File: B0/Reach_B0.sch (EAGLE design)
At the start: 149 parts, among them IC1 TMC2100-LA, IC18 74AHC1G126DCK, IC2 TMC2100-LA, IC3 74AHC1G126DCK, IC4 74AHC1G126DCK, IC5 74AHC1G126DCK, IC6 74AHC1G126DCK, IC7 74AHC1G126DCK, P8 F-2X23-, P9 F-2X23-, Q2 AON6758, Q3 AON6758, U1 SN74AHC595PW, U10 RT8268, U11 PCA9685PW, U18 CAT24C256, U2 SN74AHC595PW, U3 MCP9600, U4 MCP9600, U5 MCP9600, U6 MCP9600, X1 22-05-7028-02, X11 22-05-7028-02, X14 22-05-7048-04, X2 MSTBA4, X21 MSTBA2, X3 MSTBA2, X4 22-05-7028-02, X5 22-05-7028-02, X6 22-05-7048-04, X7 22-05-7028-02, X9 22-05-7028-02

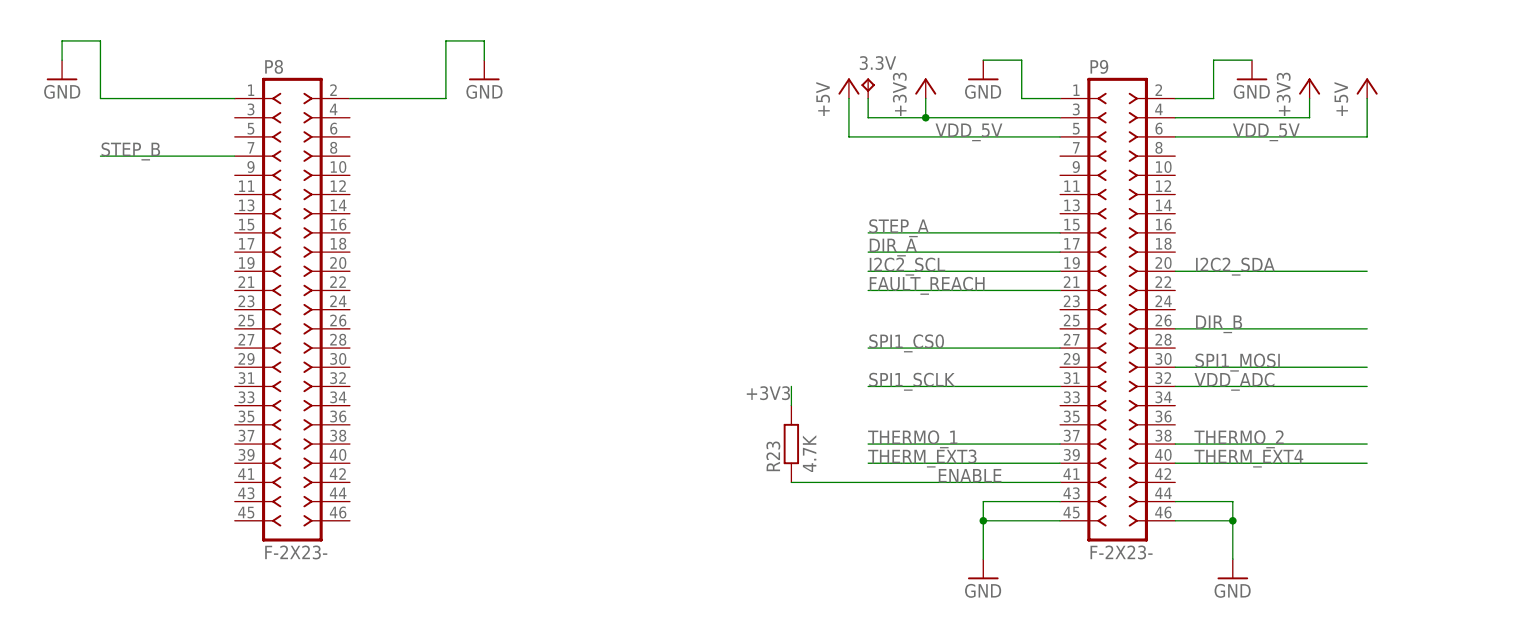
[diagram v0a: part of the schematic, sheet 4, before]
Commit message: multisheet schematic changes
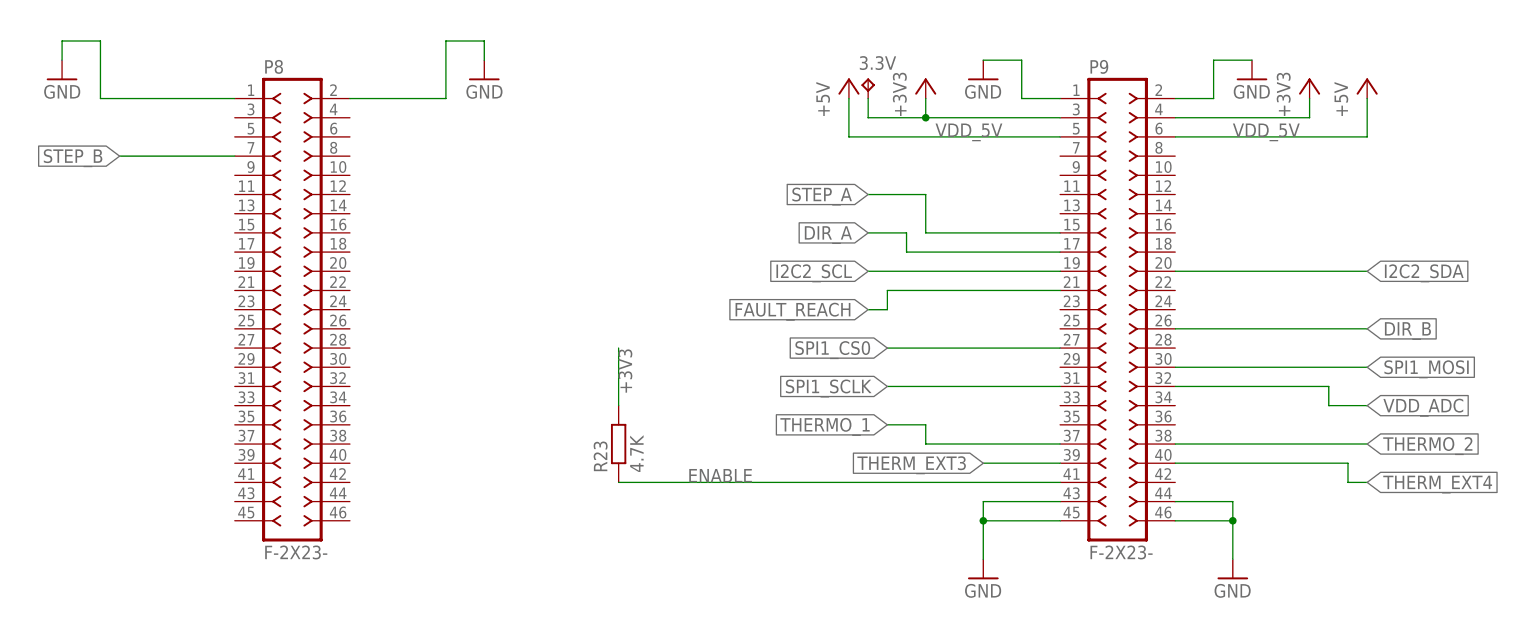
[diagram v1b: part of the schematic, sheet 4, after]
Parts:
- R13, R22, R26: value (none) -> 10k
- R16: value (none) -> 2.2k
- R24: value (none) -> 4.3k
- R27: value (none) -> 7.5k
- R7: value (none) -> DNP
- R8: value (none) -> 0
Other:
- moved on the sheet: R23
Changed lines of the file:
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@@
 <part name="GND12" library="supply1" deviceset="GND" device=""/>
 <part name="+3V8" library="supply1" deviceset="+3V3" device=""/>
-<part name="R7" library="SparkFun-Resistors" deviceset="RESISTOR" device="0402-RES"/>
-<part name="R8" library="SparkFun-Resistors" deviceset="RESISTOR" device="0402-RES"/>
+<part name="R7" library="SparkFun-Resistors" deviceset="RESISTOR" device="0402-RES" value="DNP"/>
+<part name="R8" library="SparkFun-Resistors" deviceset="RESISTOR" device="0402-RES" value="0"/>
 <part name="+3V10" library="supply1" deviceset="+3V3" device=""/>
 <part name="XTC2" library="reach_custom" deviceset="NEWPORT_THERMOCOUPLE_CONNECTOR" device="PCC-SMP-V"/>
@@
 <part name="GND13" library="supply1" deviceset="GND" device=""/>
 <part name="+3V11" library="supply1" deviceset="+3V3" device=""/>
-<part name="R13" library="SparkFun-Resistors" deviceset="RESISTOR" device="0402-RES"/>
-<part name="R16" library="SparkFun-Resistors" deviceset="RESISTOR" device="0402-RES"/>
+<part name="R13" library="SparkFun-Resistors" deviceset="RESISTOR" device="0402-RES" value="10k"/>
+<part name="R16" library="SparkFun-Resistors" deviceset="RESISTOR" device="0402-RES" value="2.2k"/>
 <part name="+3V13" library="supply1" deviceset="+3V3" device=""/>
 <part name="XTC3" library="reach_custom" deviceset="NEWPORT_THERMOCOUPLE_CONNECTOR" device="PCC-SMP-V"/>
@@
 <part name="GND30" library="supply1" deviceset="GND" device=""/>
 <part name="+3V14" library="supply1" deviceset="+3V3" device=""/>
-<part name="R22" library="SparkFun-Resistors" deviceset="RESISTOR" device="0402-RES"/>
-<part name="R24" library="SparkFun-Resistors" deviceset="RESISTOR" device="0402-RES"/>
+<part name="R22" library="SparkFun-Resistors" deviceset="RESISTOR" device="0402-RES" value="10k"/>
+<part name="R24" library="SparkFun-Resistors" deviceset="RESISTOR" device="0402-RES" value="4.3k"/>
 <part name="+3V15" library="supply1" deviceset="+3V3" device=""/>
 <part name="XTC4" library="reach_custom" deviceset="NEWPORT_THERMOCOUPLE_CONNECTOR" device="PCC-SMP-V"/>
@@
 <part name="GND33" library="supply1" deviceset="GND" device=""/>
 <part name="+3V16" library="supply1" deviceset="+3V3" device=""/>
-<part name="R26" library="SparkFun-Resistors" deviceset="RESISTOR" device="0402-RES"/>
-<part name="R27" library="SparkFun-Resistors" deviceset="RESISTOR" device="0402-RES"/>
+<part name="R26" library="SparkFun-Resistors" deviceset="RESISTOR" device="0402-RES" value="10k"/>
+<part name="R27" library="SparkFun-Resistors" deviceset="RESISTOR" device="0402-RES" value="7.5k"/>
 <part name="+3V17" library="supply1" deviceset="+3V3" device=""/>
 <part name="C9" library="rcl" deviceset="C-EU" device="C0402" value="0.1uF"/>
@@
 <instance part="P8" gate="G$1" x="63.5" y="58.42"/>
 <instance part="P9" gate="G$1" x="172.72" y="58.42"/>
-<instance part="R23" gate="G$1" x="129.54" y="40.64" rot="R90"/>
+<instance part="R23" gate="G$1" x="106.68" y="40.64" rot="R90"/>
 </instances>
 <busses>
@@
 <segment>
 <wire x1="165.1" y1="63.5" x2="139.7" y2="63.5" width="0.1524" layer="91"/>
-<label x="139.7" y="63.5" size="1.778" layer="95"/>
+<label x="139.7" y="63.5" size="1.778" layer="95" rot="R180" xref="yes"/>
 <pinref part="P9" gate="G$1" pin="19"/>
 </segment>
@@
 <segment>
 <wire x1="180.34" y1="63.5" x2="205.74" y2="63.5" width="0.1524" layer="91"/>
-<label x="182.88" y="63.5" size="1.778" layer="95"/>
+<label x="205.74" y="63.5" size="1.778" layer="95" xref="yes"/>
 <pinref part="P9" gate="G$1" pin="20"/>
 </segment>
@@
 <segment>
 <pinref part="R23" gate="G$1" pin="2"/>
-<wire x1="129.54" y1="45.72" x2="129.54" y2="48.26" width="0.1524" layer="91"/>
-<label x="129.54" y="48.26" size="1.778" layer="95" rot="R180"/>
+<wire x1="106.68" y1="45.72" x2="106.68" y2="53.34" width="0.1524" layer="91"/>
+<label x="106.68" y="53.34" size="1.778" layer="95" rot="R270"/>
 </segment>
 <segment>
@@
 <net name="SPI1_SCLK" class="0">
 <segment>
-<wire x1="165.1" y1="48.26" x2="139.7" y2="48.26" width="0.1524" layer="91"/>
-<label x="139.7" y="48.26" size="1.778" layer="95"/>
+<wire x1="165.1" y1="48.26" x2="142.24" y2="48.26" width="0.1524" layer="91"/>
+<label x="142.24" y="48.26" size="1.778" layer="95" rot="R180" xref="yes"/>
 <pinref part="P9" gate="G$1" pin="31"/>
 </segment>
@@
 <segment>
 <pinref part="P9" gate="G$1" pin="27"/>
-<wire x1="165.1" y1="53.34" x2="139.7" y2="53.34" width="0.1524" layer="91"/>
-<label x="139.7" y="53.34" size="1.778" layer="95"/>
+<wire x1="165.1" y1="53.34" x2="142.24" y2="53.34" width="0.1524" layer="91"/>
+<label x="142.24" y="53.34" size="1.778" layer="95" rot="R180" xref="yes"/>
 </segment>
 </net>
@@
 <segment>
 <pinref part="P9" gate="G$1" pin="41"/>
-<wire x1="165.1" y1="35.56" x2="129.54" y2="35.56" width="0.1524" layer="91"/>
-<label x="157.48" y="35.56" size="1.778" layer="95" rot="MR0"/>
+<wire x1="165.1" y1="35.56" x2="106.68" y2="35.56" width="0.1524" layer="91"/>
+<label x="124.46" y="35.56" size="1.778" layer="95" rot="MR0"/>
 <pinref part="R23" gate="G$1" pin="1"/>
 </segment>
@@
 <segment>
 <wire x1="180.34" y1="50.8" x2="205.74" y2="50.8" width="0.1524" layer="91"/>
-<label x="182.88" y="50.8" size="1.778" layer="95"/>
+<label x="205.74" y="50.8" size="1.778" layer="95" xref="yes"/>
 <pinref part="P9" gate="G$1" pin="30"/>
 </segment>
@@
 <net name="VDD_ADC" class="0">
 <segment>
-<wire x1="180.34" y1="48.26" x2="205.74" y2="48.26" width="0.1524" layer="91"/>
-<label x="182.88" y="48.26" size="1.778" layer="95"/>
+<label x="205.74" y="45.72" size="1.778" layer="95" xref="yes"/>
 <pinref part="P9" gate="G$1" pin="32"/>
+<wire x1="180.34" y1="48.26" x2="200.66" y2="48.26" width="0.1524" layer="91"/>
+<wire x1="200.66" y1="48.26" x2="200.66" y2="45.72" width="0.1524" layer="91"/>
+<wire x1="200.66" y1="45.72" x2="205.74" y2="45.72" width="0.1524" layer="91"/>
 </segment>
 </net>
@@
 <segment>
 <pinref part="P9" gate="G$1" pin="21"/>
-<wire x1="165.1" y1="60.96" x2="139.7" y2="60.96" width="0.1524" layer="91"/>
-<label x="139.7" y="60.96" size="1.778" layer="95"/>
+<label x="139.7" y="58.42" size="1.778" layer="95" rot="R180" xref="yes"/>
+<wire x1="165.1" y1="60.96" x2="142.24" y2="60.96" width="0.1524" layer="91"/>
+<wire x1="142.24" y1="60.96" x2="142.24" y2="58.42" width="0.1524" layer="91"/>
+<wire x1="142.24" y1="58.42" x2="139.7" y2="58.42" width="0.1524" layer="91"/>
 </segment>
 </net>
@@
 <pinref part="P9" gate="G$1" pin="26"/>
 <wire x1="180.34" y1="55.88" x2="205.74" y2="55.88" width="0.1524" layer="91"/>
-<label x="182.88" y="55.88" size="1.778" layer="95"/>
+<label x="205.74" y="55.88" size="1.778" layer="95" xref="yes"/>
 </segment>
 </net>
@@
 <segment>
 <pinref part="P8" gate="G$1" pin="7"/>
-<wire x1="55.88" y1="78.74" x2="38.1" y2="78.74" width="0.1524" layer="91"/>
-<label x="38.1" y="78.74" size="1.778" layer="95"/>
+<wire x1="55.88" y1="78.74" x2="40.64" y2="78.74" width="0.1524" layer="91"/>
+<label x="40.64" y="78.74" size="1.778" layer="95" rot="R180" xref="yes"/>
 </segment>
 </net>
@@
 <segment>
 <pinref part="P9" gate="G$1" pin="15"/>
-<wire x1="165.1" y1="68.58" x2="139.7" y2="68.58" width="0.1524" layer="91"/>
-<label x="139.7" y="68.58" size="1.778" layer="95"/>
+<label x="139.7" y="73.66" size="1.778" layer="95" rot="R180" xref="yes"/>
+<wire x1="165.1" y1="68.58" x2="147.32" y2="68.58" width="0.1524" layer="91"/>
+<wire x1="147.32" y1="68.58" x2="147.32" y2="73.66" width="0.1524" layer="91"/>
+<wire x1="147.32" y1="73.66" x2="139.7" y2="73.66" width="0.1524" layer="91"/>
 </segment>
 </net>
@@
 <segment>
 <pinref part="P9" gate="G$1" pin="17"/>
-<wire x1="165.1" y1="66.04" x2="139.7" y2="66.04" width="0.1524" layer="91"/>
-<label x="139.7" y="66.04" size="1.778" layer="95"/>
+<label x="139.7" y="68.58" size="1.778" layer="95" rot="R180" xref="yes"/>
+<wire x1="165.1" y1="66.04" x2="144.78" y2="66.04" width="0.1524" layer="91"/>
+<wire x1="144.78" y1="66.04" x2="144.78" y2="68.58" width="0.1524" layer="91"/>
+<wire x1="144.78" y1="68.58" x2="139.7" y2="68.58" width="0.1524" layer="91"/>
 </segment>
 </net>
@@
 <segment>
 <pinref part="P9" gate="G$1" pin="39"/>
-<wire x1="165.1" y1="38.1" x2="139.7" y2="38.1" width="0.1524" layer="91"/>
-<label x="139.7" y="38.1" size="1.778" layer="95"/>
+<wire x1="165.1" y1="38.1" x2="154.94" y2="38.1" width="0.1524" layer="91"/>
+<label x="154.94" y="38.1" size="1.778" layer="95" rot="R180" xref="yes"/>
 </segment>
 </net>
@@
 <segment>
 <pinref part="P9" gate="G$1" pin="40"/>
-<wire x1="180.34" y1="38.1" x2="205.74" y2="38.1" width="0.1524" layer="91"/>
-<label x="182.88" y="38.1" size="1.778" layer="95"/>
+<label x="205.74" y="35.56" size="1.778" layer="95" xref="yes"/>
+<wire x1="180.34" y1="38.1" x2="203.2" y2="38.1" width="0.1524" layer="91"/>
+<wire x1="203.2" y1="38.1" x2="203.2" y2="35.56" width="0.1524" layer="91"/>
+<wire x1="203.2" y1="35.56" x2="205.74" y2="35.56" width="0.1524" layer="91"/>
 </segment>
 </net>
@@
 <segment>
 <pinref part="P9" gate="G$1" pin="37"/>
-<wire x1="165.1" y1="40.64" x2="139.7" y2="40.64" width="0.1524" layer="91"/>
-<label x="139.7" y="40.64" size="1.778" layer="95"/>
+<label x="142.24" y="43.18" size="1.778" layer="95" rot="R180" xref="yes"/>
+<wire x1="165.1" y1="40.64" x2="147.32" y2="40.64" width="0.1524" layer="91"/>
+<wire x1="147.32" y1="40.64" x2="147.32" y2="43.18" width="0.1524" layer="91"/>
+<wire x1="147.32" y1="43.18" x2="142.24" y2="43.18" width="0.1524" layer="91"/>
 </segment>
 </net>
@@
 <pinref part="P9" gate="G$1" pin="38"/>
 <wire x1="180.34" y1="40.64" x2="205.74" y2="40.64" width="0.1524" layer="91"/>
-<label x="182.88" y="40.64" size="1.778" layer="95"/>
+<label x="205.74" y="40.64" size="1.778" layer="95" xref="yes"/>
 </segment>
 </net>
@@
 </sheet>
 </sheets>
+<errors>
+</errors>
 </schematic>
 </drawing>

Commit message: stepper drivers laid out
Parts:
- added C31, C34, C37, C40: 4.7uF, rcl:C-EUC0402
- added C32: 22nF, rcl:C-EUC0402
- added C33, C35, C36, C38, C39, C42, C43, C44: 0.1uF, rcl:C-EUC0402
- added C47: 10uF, rcl:C-EUC0805
- added C48: 100uF, Panasonic-EEEFK_EEEFP:C
- added IC10, IC11, IC9: 74AHC1G126DCK, 74xx-little-de:74AHC1G126DCK
- added IC8: TMC2100-LA, we-chip:TMC2100-LA
- added R28: 10k, rcl:R-EU_R0402
- added R29: 7.5k, rcl:R-EU_R0402
- added R30: 4.3k, rcl:R-EU_R0402
- added R31, R35: 0.1R, rcl:R-EU_R0805
- added R36, R46: 10K, rcl:R-EU_R0402
- added R37: 4.7K, rcl:R-EU_R0402
- added R38: 2.2R, rcl:R-EU_R0402
- added U7: SN74AHC595PW, sn74hc595:SN74AHC595PW
- added X8: 22-05-7048-04, con-molex:22-05-7048-04
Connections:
- removed net THERMO_1: P9.37
- new net DIR_C: IC8.REFR_DIR, P9.29
- new net ENABLE_C: IC11A.O, IC8.DRV_ENN_CFG6
- new net IREF_C_RAW: R46.2, U11.LED13
- new net IREF_X2: C40.1, R36.2, R46.1
- new net N$52: C32.2, IC8.CPO
- new net N$53: R29.1, R30.2
- new net N$54: IC8.BRB, R31.2
- new net N$55: IC8.BRA, R35.2
- new net N$56: C34.1, IC8.AIN_IREF, R36.1
- new net N$57: C32.1, IC8.CPI
- new net N$58: C37.2, IC8.5VOUT, R38.1
- new net N$59: C38.1, IC8.VCP
- new net N$60: IC8.ENCB_DCEN_CFG4, U7.QC
- new net N$61: IC8.ENCA_DCIN_CFG5, U7.QB
- new net N$62: IC10A.OE, U7.QH
- new net N$63: IC10A.I, U7.QG
- new net N$65: IC9A.I, U7.QE
- new net N$66: IC9A.OE, U7.QF
- new net N$67: IC8.SDO_NAO_CFG0, U7.QD
- new net N$68: C39.1, IC8.VCC, R38.2
- new net N$69: IC11A.I, U7.QA
- new net N$9: C17.1, U11.VDD
- new net STEP_C: IC8.REFL_STEP, P9.21
- new net X_A5: IC8.OA1, X8-2.S
- new net X_A6: IC8.OA2, X8-1.S
- new net X_B5: IC8.OB2, X8-4.S
- new net X_B6: IC8.OB1, X8-3.S
- new net X_CFG5: IC8.SCK_CFG2, IC9A.O
- new net X_CFG6: IC10A.O, IC8.SDI_NAI_CFG1
- net +3V3: now also C33.1, C35.1, C42.1, IC10P.VCC, IC11P.VCC, IC8.VCC_IO, IC9P.VCC, R37.2, U7.VCC, U7.~SRCLR
- net DIR_A: now also IC1.REFR_DIR; no longer IC2.REFR_DIR
- net DIR_B: now also IC2.REFR_DIR; no longer IC1.REFR_DIR
- net FAULT_REACH: now also C31.1, P9.37, R28.1, R29.2; no longer P9.21
- net FAULT_X: now also IC8.SWN_DIAG0, R28.2, R37.1
- net GND: now also C31.2, C33.2, C34.2, C35.2, C36.1, C37.1, C39.2, C40.2, C42.2, C43.2, C44.2, C47.2, C48.-, IC10P.GND, IC11P.GND, IC8.CLK, IC8.GND, IC8.GNDA, IC8.SPI_MODE, IC8.TST_MODE, IC9P.GND, R30.1, R31.1, R35.1, U7.GND, U7.~OE
- net IREF_A_RAW: now also R41.2; no longer R12.2
- net IREF_B_RAW: now also R12.2; no longer R41.2
- net SER_2: now also U7.QH_2
- net SPI1_CS0: now also U7.RCLK; no longer P9.27
- net SPI1_MOSI: now also U7.SER
- net SPI1_SCLK: now also U7.SRCLK
- net STEP_A: now also IC1.REFL_STEP; no longer IC2.REFL_STEP
- net STEP_B: now also IC2.REFL_STEP; no longer IC1.REFL_STEP
- net TRISTATE_STEPPERS: now also IC11A.OE
- net VDD_5V: no longer C17.1, U11.VDD
- net VDD_IN: now also C36.2, C38.2, C43.1, C44.1, C47.1, C48.+, IC8.VS, IC8.VSA
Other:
- note added: "A axis"
- note added: "B axis"
- note added: "Beaglebone Black Connectors"
- note added: "C Axis"
- note added: "Fault level shift"
- note removed: "TERM_EXT3"
- note removed: "TERM_EXT4"
